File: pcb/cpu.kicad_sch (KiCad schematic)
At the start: 30 parts, among them J19 Conn_01x02_Pin, J20 Conn_01x02_Pin, J21 Conn_01x02_Pin, J22 Conn_01x02_Pin, J3 ATX-20, J9 CLKMUL SET, SW1 SW_SPDT, U1 486Socket, U19 74LS245, U20 74LS245, U5 74LS245, U6 74LS245, U7 74LS245, U8 74LS245

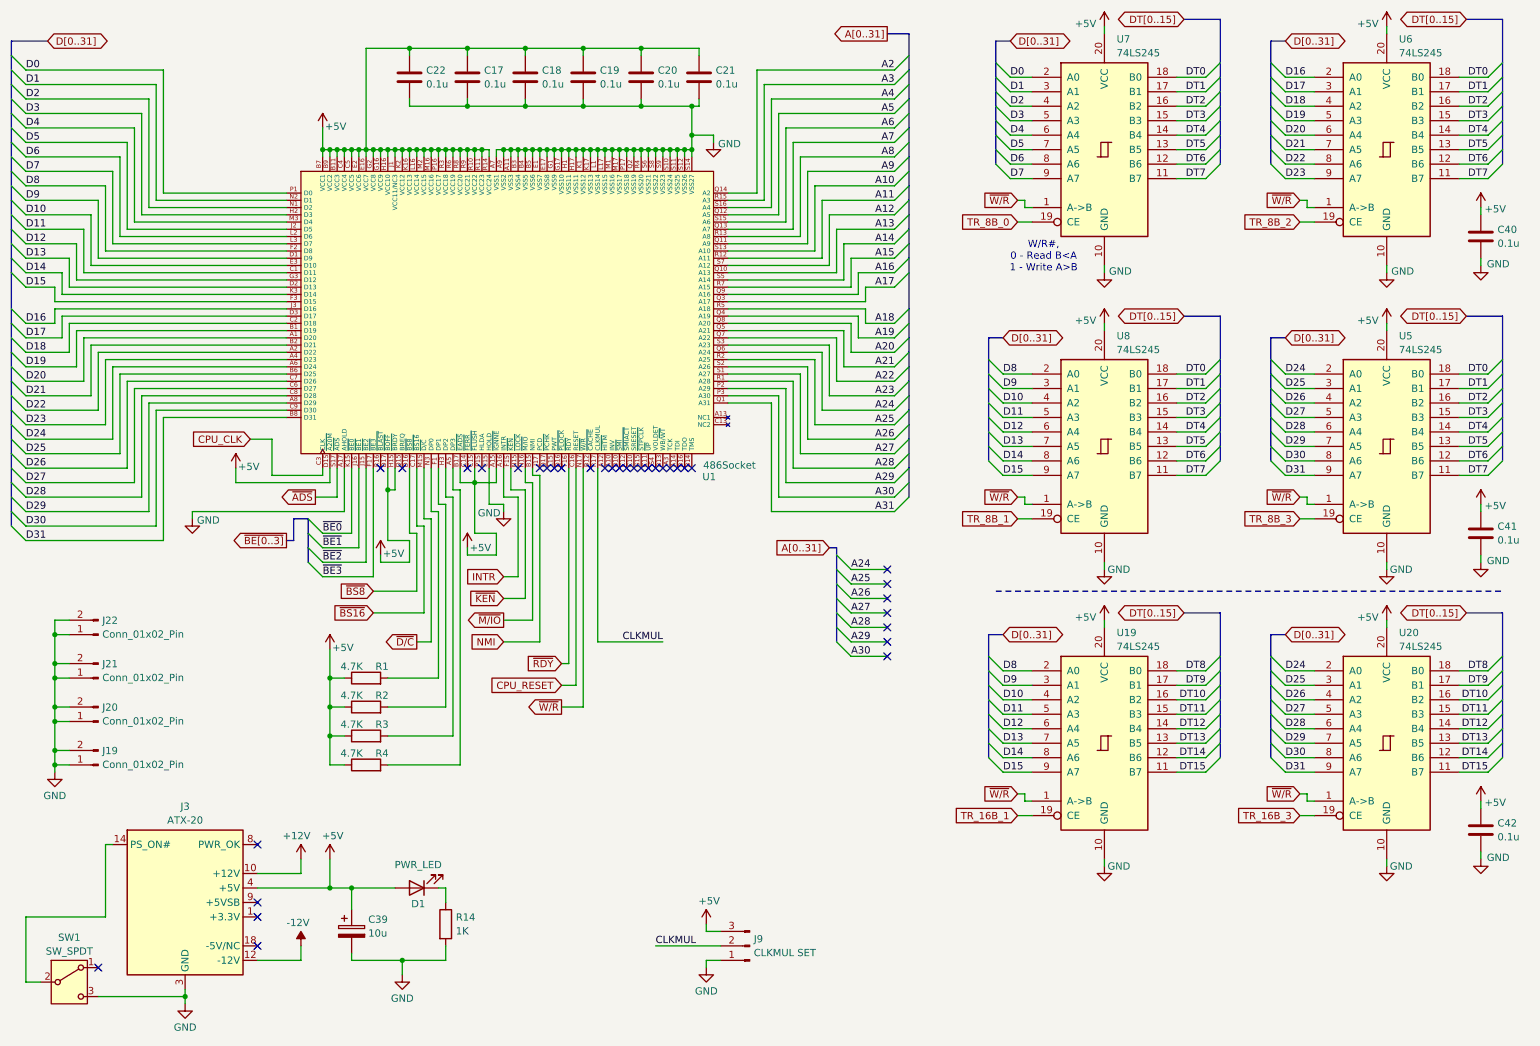
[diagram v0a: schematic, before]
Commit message: Add fpga sources, update schematic, update README
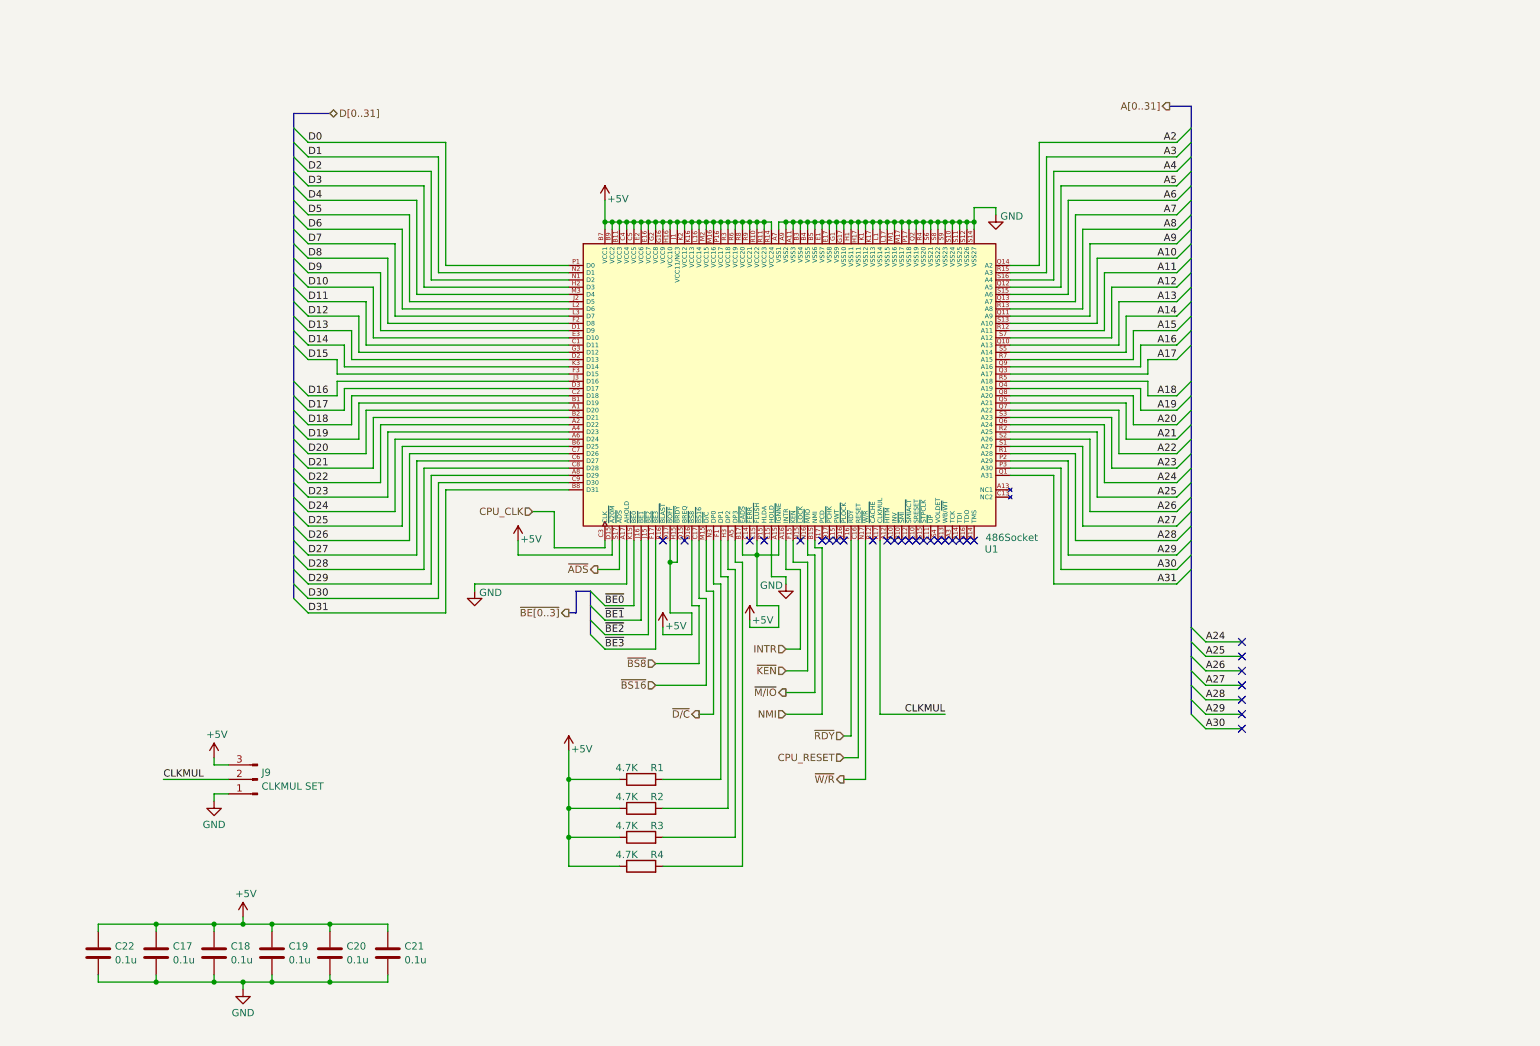
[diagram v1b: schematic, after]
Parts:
- removed C39: 10u, Capacitor_THT:CP_Radial_D5.0mm_P2.50mm, symbol Device:C_Polarized
- removed C40, C41, C42: 0.1u, Capacitor_SMD:C_0805_2012Metric_Pad1.18x1.45mm_HandSolder, symbol Device:C
- removed D1: PWR_LED, LED_THT:LED_D4.0mm, symbol Device:LED
- removed J19, J20, J21, J22: Conn_01x02_Pin, Connector_PinHeader_2.54mm:PinHeader_1x02_P2.54mm_Vertical, symbol Connector:Conn_01x02_Pin
- removed J3: ATX-20, Connector_Molex:Molex_Mini-Fit_Jr_5566-20A_2x10_P4.20mm_Vertical, symbol Connector:ATX-20
- removed R14: 1K, Resistor_SMD:R_0805_2012Metric_Pad1.20x1.40mm_HandSolder, symbol Device:R
- removed SW1: SW_SPDT, Connector_PinHeader_2.54mm:PinHeader_1x03_P2.54mm_Vertical, symbol Switch:SW_SPDT
- removed U19, U20, U5, U6, U7, U8: 74LS245, Package_SO:SOP-20_7.5x12.8mm_P1.27mm, symbol 74xx:74LS245
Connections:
- no-connect marks 35 -> 30
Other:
- note removed: "W/R#, 0 - Read B<A 1 - Write A>B"
- moved on the sheet: C17, C18, C19, C20, C21, C22, J9, R1, R2, R3, R4, U1

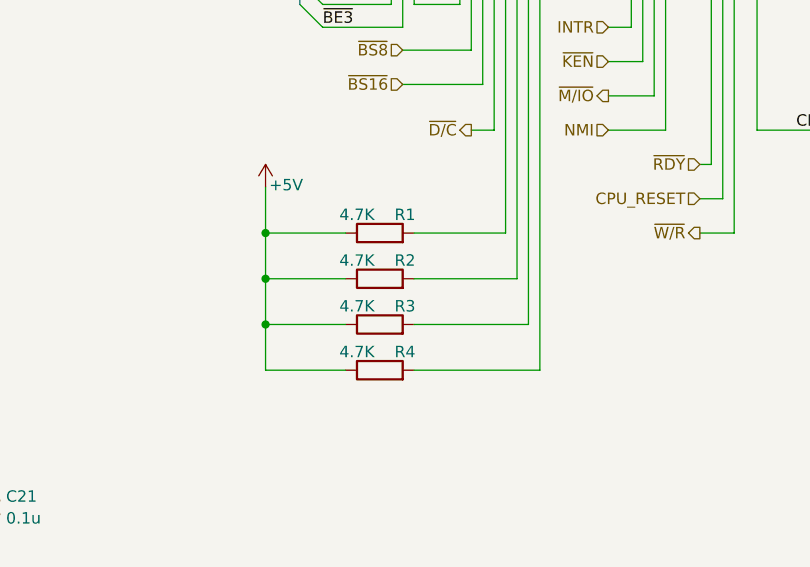
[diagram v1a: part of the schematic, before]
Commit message: 1052 vias down to 917, had to reshuffle some resistors and connectors
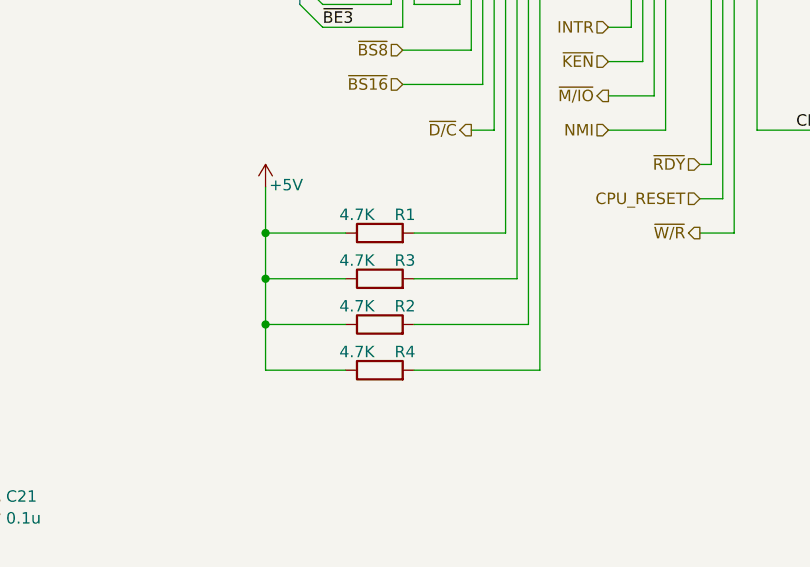
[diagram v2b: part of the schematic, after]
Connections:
- net at U1.F1 (DP1): now also R3.2; no longer R2.2
- net at U1.H3 (DP2): now also R2.2; no longer R3.2
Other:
- moved on the sheet: R2, R3
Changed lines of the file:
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@@
 	)
 	(junction
-		(at 113.03 157.48)
-		(diameter 0)
-		(color 0 0 0 0)
-	)
-	(junction
 		(at 121.92 49.53)
 		(diameter 0)
@@
 	)
 	(junction
+		(at 113.03 152.4)
+		(diameter 0)
+		(color 0 0 0 0)
+	)
+	(junction
 		(at 165.1 49.53)
 		(diameter 0)
@@
 	)
 	(junction
-		(at 113.03 152.4)
-		(diameter 0)
-		(color 0 0 0 0)
-	)
-	(junction
 		(at 119.38 49.53)
 		(diameter 0)
@@
 		(color 0 0 0 0)
 	)
+	(junction
+		(at 113.03 157.48)
+		(diameter 0)
+		(color 0 0 0 0)
+	)
 	(no_connect
 		(at 231.14 138.43)
@@
 	(wire
 		(pts
-			(xy 113.03 152.4) (xy 121.92 152.4)
+			(xy 113.03 157.48) (xy 121.92 157.48)
 		)
 		(stroke
@@
 	(wire
 		(pts
+			(xy 113.03 152.4) (xy 113.03 157.48)
+		)
+		(stroke
+			(width 0)
+			(type default)
+		)
+	)
+	(wire
+		(pts
 			(xy 134.62 121.92) (xy 129.54 121.92)
 		)
@@
 	(wire
 		(pts
-			(xy 129.54 152.4) (xy 140.97 152.4)
+			(xy 129.54 157.48) (xy 142.24 157.48)
 		)
 		(stroke
@@
 	(wire
 		(pts
-			(xy 129.54 157.48) (xy 142.24 157.48)
+			(xy 129.54 152.4) (xy 140.97 152.4)
 		)
 		(stroke
@@
 	(wire
 		(pts
-			(xy 113.03 157.48) (xy 121.92 157.48)
+			(xy 113.03 152.4) (xy 121.92 152.4)
 		)
 		(stroke
@@
 	(wire
 		(pts
-			(xy 113.03 157.48) (xy 113.03 162.56)
-		)
-		(stroke
-			(width 0)
-			(type default)
-		)
-	)
-	(wire
-		(pts
 			(xy 139.7 105.41) (xy 139.7 111.76)
 		)
@@
 	(wire
 		(pts
-			(xy 113.03 147.32) (xy 113.03 152.4)
-		)
-		(stroke
-			(width 0)
-			(type default)
-		)
-	)
-	(wire
-		(pts
 			(xy 203.2 88.9) (xy 203.2 102.87)
 		)
@@
 	(wire
 		(pts
-			(xy 113.03 152.4) (xy 113.03 157.48)
-		)
-		(stroke
-			(width 0)
-			(type default)
-		)
-	)
-	(wire
-		(pts
 			(xy 127 121.92) (xy 119.38 121.92)
 		)
@@
 		)
 	)
+	(wire
+		(pts
+			(xy 113.03 147.32) (xy 113.03 152.4)
+		)
+		(stroke
+			(width 0)
+			(type default)
+		)
+	)
 	(bus
 		(pts
@@
 	(wire
 		(pts
-			(xy 176.53 49.53) (xy 176.53 50.8)
+			(xy 113.03 157.48) (xy 113.03 162.56)
 		)
 		(stroke
@@
 	(wire
 		(pts
-			(xy 140.97 152.4) (xy 140.97 111.76)
+			(xy 176.53 49.53) (xy 176.53 50.8)
 		)
 		(stroke
@@
 	(wire
 		(pts
+			(xy 140.97 152.4) (xy 140.97 111.76)
+		)
+		(stroke
+			(width 0)
+			(type default)
+		)
+	)
+	(wire
+		(pts
 			(xy 71.12 181.61) (xy 71.12 182.88)
 		)
@@
 	(symbol
 		(lib_id "Device:R")
-		(at 125.73 157.48 90)
+		(at 125.73 152.4 90)
 		(unit 1)
 		(exclude_from_sim no)
@@
 		(dnp no)
 		(property "Reference" "R3"
-			(at 128.524 155.448 90)
+			(at 128.524 150.368 90)
 			(effects
 				(font
@@
 		)
 		(property "Value" "4.7K"
-			(at 123.19 155.448 90)
+			(at 123.19 150.368 90)
 			(effects
 				(font
@@
 		)
 		(property "Footprint" "Resistor_SMD:R_0805_2012Metric_Pad1.20x1.40mm_HandSolder"
-			(at 125.73 159.258 90)
+			(at 125.73 154.178 90)
 			(effects
 				(font
@@
 		)
 		(property "Datasheet" "~"
-			(at 125.73 157.48 0)
+			(at 125.73 152.4 0)
 			(effects
 				(font
@@
 		)
 		(property "Description" "Resistor"
-			(at 125.73 157.48 0)
+			(at 125.73 152.4 0)
 			(effects
 				(font
@@
 	(symbol
 		(lib_id "Device:R")
-		(at 125.73 152.4 90)
+		(at 125.73 157.48 90)
 		(unit 1)
 		(exclude_from_sim no)
@@
 		(dnp no)
 		(property "Reference" "R2"
-			(at 128.524 150.368 90)
+			(at 128.524 155.448 90)
 			(effects
 				(font
@@
 		)
 		(property "Value" "4.7K"
-			(at 123.19 150.368 90)
+			(at 123.19 155.448 90)
 			(effects
 				(font
@@
 		)
 		(property "Footprint" "Resistor_SMD:R_0805_2012Metric_Pad1.20x1.40mm_HandSolder"
-			(at 125.73 154.178 90)
+			(at 125.73 159.258 90)
 			(effects
 				(font
@@
 		)
 		(property "Datasheet" "~"
-			(at 125.73 152.4 0)
+			(at 125.73 157.48 0)
 			(effects
 				(font
@@
 		)
 		(property "Description" "Resistor"
-			(at 125.73 152.4 0)
+			(at 125.73 157.48 0)
 			(effects
 				(font

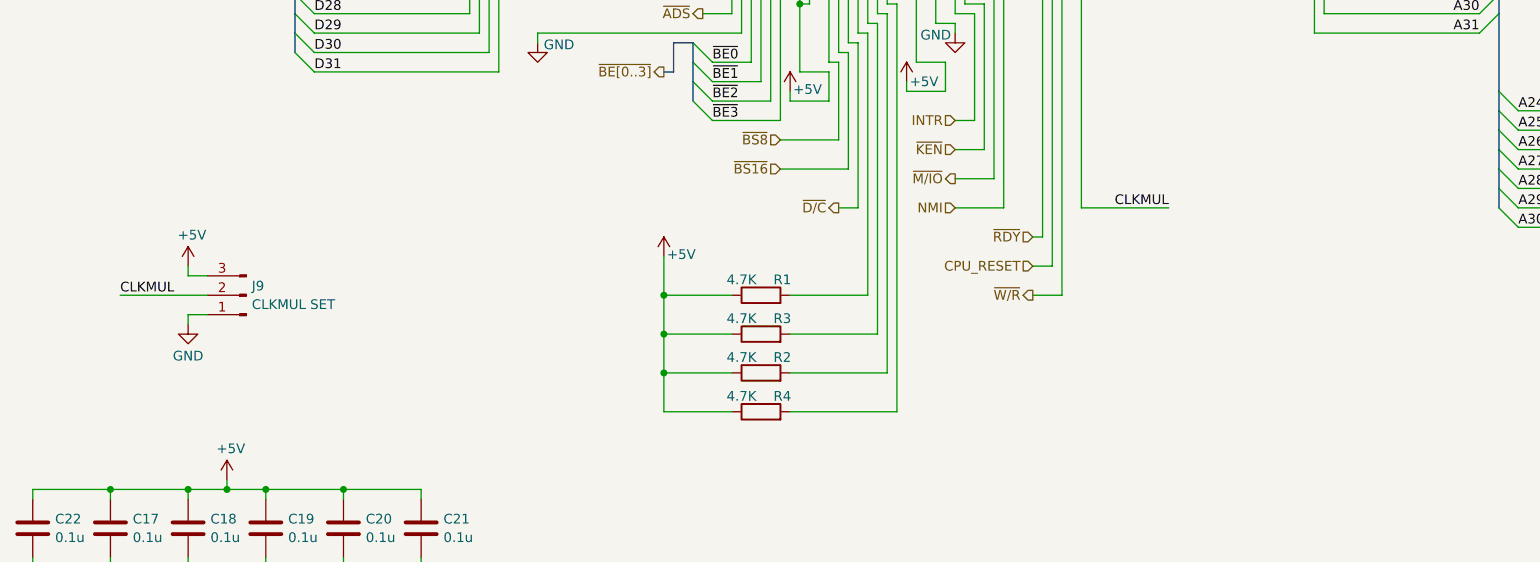
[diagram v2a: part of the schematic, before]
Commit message: added two additional 47uF CPU decoupling caps
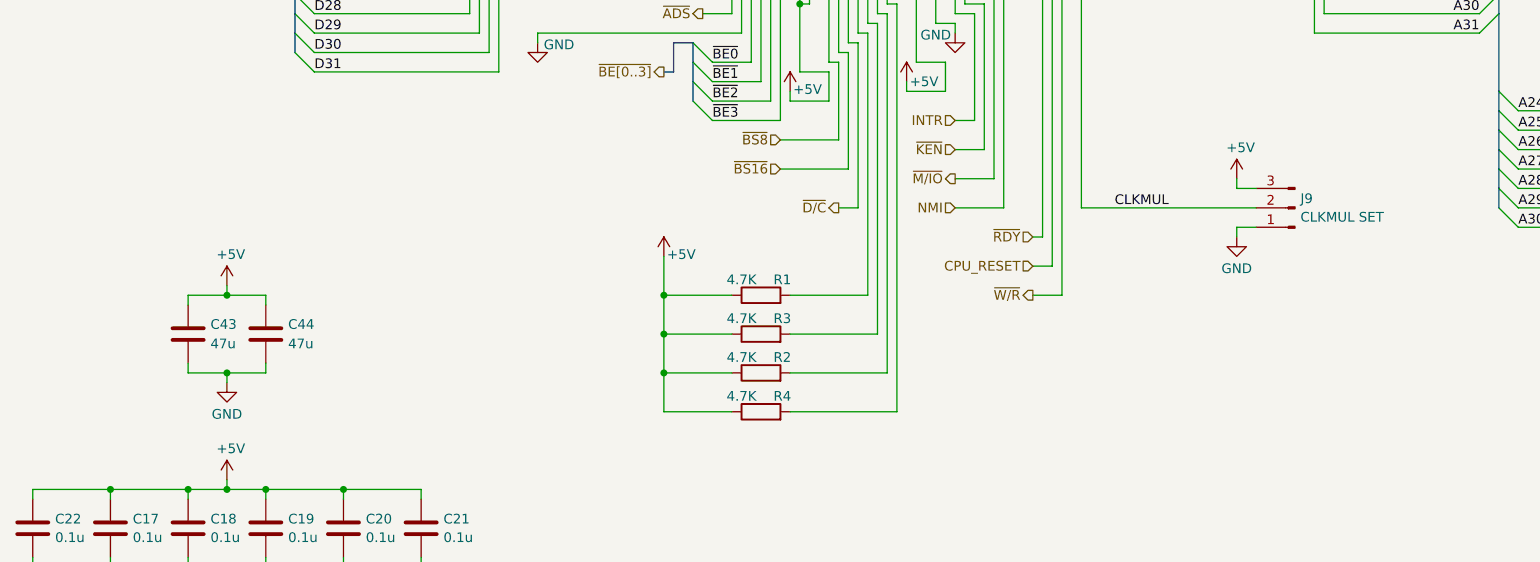
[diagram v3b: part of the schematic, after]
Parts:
- added C43, C44: 47u, Capacitor_SMD:C_1210_3225Metric, symbol Device:C
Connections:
- net +5V: now also C43.2, C44.2
- net GND: now also C43.1, C44.1
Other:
- moved on the sheet: J9
